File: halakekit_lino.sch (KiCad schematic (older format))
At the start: 8 parts, among them J1 HEADER_3, J2 HEADER_3, J3 HEADER_3, J4 HEADER_3, U1 BCM20737S

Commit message: Change board layout as rev 1.2
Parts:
- removed J1, J2, J3, J4: HEADER_3, simple_headers:Pin_Header_Straight_1x03_circle, symbol HEADER_3
- added J1: HEADER_10, simple_headers:Pin_Header_Straight_1x10, symbol HEADER_10
- 100u1: footprint Capacitors_SMD:C_0201 -> register_and_condensor:C_0603
- 10K1: footprint Resistors_SMD:R_0201 -> register_and_condensor:R_0603
- BT1: footprint CR2032_frame:BC-2001(CR2032 frame) -> CR2032_frame:BAT-HLD-001-TRCT
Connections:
- net GND: now also J1.5
- net RX: now also U1.31 (P2), J1.10; no longer U1.18 (UART_RX)
- net TX: now also U1.28 (P0), J1.9; no longer U1.19 (UART_TX)
- net VCC: now also J1.3
- net A1: now reaches U1.35 (P32)
- net A1: now also J1.8
- net AIO renamed A0
- net A0: now also J1.7
- net PIO0 renamed D0
- net D0: now also J1.6
- net PIO1 renamed D1
- net D1: now also J1.4
- net RST: no longer names the net of U1.27 (RESET_N)
- new net FWRX: J1.2, U1.18 (UART_RX)
- new net FWTX: J1.1, U1.19 (UART_TX)
- no-connect marks 17 -> 15
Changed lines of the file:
@@
 EESchema Schematic File Version 2
+LIBS:halakekit_lino-rescue
 LIBS:power
 LIBS:device
@@
 encoding utf-8
 Sheet 1 1
-Title ""
-Date ""
-Rev ""
-Comp ""
-Comment1 ""
+Title "HaLakeKit Lino"
+Date "2016-12-27"
+Rev "2.0"
+Comp "Nyampass.co.ltd"
+Comment1 "http://nyampass.com"
 Comment2 ""
 Comment3 ""
@@
 	1    0    0    -1
 $EndComp
-$Comp
-L BCM20737S U1
-U 1 1 583F77A8
-P 5100 2900
-F 0 "U1" H 5200 800 60  0000 C CNN
-F 1 "BCM20737S" H 5200 3300 60  0000 C CNN
-F 2 "BCM20737S:BCM20737S" H 5100 2900 60  0001 C CNN
-F 3 "" H 5100 2900 60  0000 C CNN
-	1    5100 2900
-	1    0    0    -1
-$EndComp
 Text GLabel 4550 4300 0    39   Input ~ 0
-RX
+FWRX
 Text GLabel 4550 4400 0    39   Input ~ 0
-TX
+FWTX
 NoConn ~ 5850 3600
 NoConn ~ 4550 3500
@@
 NoConn ~ 4550 4700
 NoConn ~ 5850 4800
-Text GLabel 5850 4700 2    39   Input ~ 0
-RST
 $Comp
 L GND #PWR02
@@
 F 0 "10K1" V 6180 4900 50  0000 C CNN
 F 1 "R" V 6100 4900 50  0000 C CNN
-F 2 "Resistors_SMD:R_0201" V 6030 4900 50  0001 C CNN
+F 2 "register_and_condensor:R_0603" V 6030 4900 50  0001 C CNN
 F 3 "" H 6100 4900 50  0000 C CNN
 	1    6100 4900
@@
 $EndComp
 Text GLabel 4550 2600 0    39   Input ~ 0
-PIO1
+D1
 Text GLabel 5850 3200 2    39   Input ~ 0
-PIO0
+D0
 Text GLabel 5850 3400 2    39   Input ~ 0
-AIO
+A0
 NoConn ~ 5850 3000
 NoConn ~ 5850 3100
-NoConn ~ 5850 3500
 NoConn ~ 5850 3700
 NoConn ~ 5850 3800
-NoConn ~ 5850 3900
-NoConn ~ 5850 4000
 NoConn ~ 5850 4100
 NoConn ~ 5850 4200
-NoConn ~ 5850 4300
 NoConn ~ 5850 4400
-NoConn ~ 5850 4600
 $Comp
 L VCC #PWR06
@@
 F 0 "100u1" H 7125 5000 50  0000 L CNN
 F 1 "C" H 7125 4800 50  0000 L CNN
-F 2 "Capacitors_SMD:C_0201" H 7138 4750 50  0001 C CNN
+F 2 "register_and_condensor:C_0603" H 7138 4750 50  0001 C CNN
 F 3 "" H 7100 4900 50  0000 C CNN
 	1    7100 4900
-	1    0    0    -1
-$EndComp
-$Comp
-L HEADER_3 J1
-U 1 1 583FB57F
-P 7700 3350
-F 0 "J1" H 7700 3550 60  0000 C CNN
-F 1 "HEADER_3" H 7700 3150 60  0000 C CNN
-F 2 "simple_headers:Pin_Header_Straight_1x03_circle" H 7700 3350 60  0001 C CNN
-F 3 "" H 7700 3350 60  0000 C CNN
-	1    7700 3350
 	1    0    0    -1
 $EndComp
@@
 F 0 "BT1" H 8050 4950 50  0000 L CNN
 F 1 "Battery" H 8050 4850 50  0000 L CNN
-F 2 "CR2032_frame:BC-2001(CR2032 frame)" V 7950 4940 50  0001 C CNN
+F 2 "CR2032_frame:BAT-HLD-001-TRCT" V 7950 4940 50  0001 C CNN
 F 3 "" V 7950 4940 50  0000 C CNN
 	1    7950 4900
@@
 	1    0    0    -1
 $EndComp
-$Comp
-L HEADER_3 J2
-U 1 1 583FB793
-P 7700 3950
-F 0 "J2" H 7700 4150 60  0000 C CNN
-F 1 "HEADER_3" H 7700 3750 60  0000 C CNN
-F 2 "simple_headers:Pin_Header_Straight_1x03_circle" H 7700 3950 60  0001 C CNN
-F 3 "" H 7700 3950 60  0000 C CNN
-	1    7700 3950
-	1    0    0    -1
-$EndComp
-$Comp
-L HEADER_3 J3
-U 1 1 583FB7D1
-P 8300 3350
-F 0 "J3" H 8300 3550 60  0000 C CNN
-F 1 "HEADER_3" H 8300 3150 60  0000 C CNN
-F 2 "simple_headers:Pin_Header_Straight_1x03_circle" H 8300 3350 60  0001 C CNN
-F 3 "" H 8300 3350 60  0000 C CNN
-	1    8300 3350
-	1    0    0    -1
-$EndComp
-$Comp
-L HEADER_3 J4
-U 1 1 583FB80E
-P 8600 3950
-F 0 "J4" H 8600 4150 60  0000 C CNN
-F 1 "HEADER_3" H 8600 3750 60  0000 C CNN
-F 2 "simple_headers:Pin_Header_Straight_1x03_circle" H 8600 3950 60  0001 C CNN
-F 3 "" H 8600 3950 60  0000 C CNN
-	1    8600 3950
-	1    0    0    -1
-$EndComp
-Text GLabel 7600 3450 0    39   Input ~ 0
+Text GLabel 8500 3150 0    39   Input ~ 0
+FWTX
+Text GLabel 8500 3250 0    39   Input ~ 0
+FWRX
+Text GLabel 8500 3750 0    39   Input ~ 0
+A0
+Text GLabel 8500 3850 0    39   Input ~ 0
+A1
+Text GLabel 8500 3950 0    39   Input ~ 0
 TX
-Text GLabel 7600 3350 0    39   Input ~ 0
-RX
-Text GLabel 7600 3250 0    39   Input ~ 0
-RST
-Text GLabel 8200 3250 0    39   Input ~ 0
-PIO1
-Text GLabel 8200 3350 0    39   Input ~ 0
-PIO0
-Text GLabel 8200 3450 0    39   Input ~ 0
-AIO
 $Comp
 L VCC #PWR010
 U 1 1 583FB8FE
-P 7300 3850
-F 0 "#PWR010" H 7300 3700 50  0001 C CNN
-F 1 "VCC" H 7300 4000 50  0000 C CNN
-F 2 "" H 7300 3850 50  0000 C CNN
-F 3 "" H 7300 3850 50  0000 C CNN
-	1    7300 3850
+P 8200 3350
+F 0 "#PWR010" H 8200 3200 50  0001 C CNN
+F 1 "VCC" H 8200 3500 50  0000 C CNN
+F 2 "" H 8200 3350 50  0000 C CNN
+F 3 "" H 8200 3350 50  0000 C CNN
+	1    8200 3350
 	1    0    0    -1
 $EndComp
 $Comp
 L GND #PWR011
-U 1 1 583FB954
-P 8300 4100
-F 0 "#PWR011" H 8300 3850 50  0001 C CNN
-F 1 "GND" H 8300 3950 50  0000 C CNN
-F 2 "" H 8300 4100 50  0000 C CNN
-F 3 "" H 8300 4100 50  0000 C CNN
-	1    8300 4100
-	1    0    0    -1
-$EndComp
-$Comp
-L VCC #PWR012
-U 1 1 583FB9BD
-P 8300 3850
-F 0 "#PWR012" H 8300 3700 50  0001 C CNN
-F 1 "VCC" H 8300 4000 50  0000 C CNN
-F 2 "" H 8300 3850 50  0000 C CNN
-F 3 "" H 8300 3850 50  0000 C CNN
-	1    8300 3850
-	1    0    0    -1
-$EndComp
-$Comp
-L GND #PWR013
 U 1 1 583FB9E0
-P 7300 4100
-F 0 "#PWR013" H 7300 3850 50  0001 C CNN
-F 1 "GND" H 7300 3950 50  0000 C CNN
-F 2 "" H 7300 4100 50  0000 C CNN
-F 3 "" H 7300 4100 50  0000 C CNN
-	1    7300 4100
+P 8200 3550
+F 0 "#PWR011" H 8200 3300 50  0001 C CNN
+F 1 "GND" H 8200 3400 50  0000 C CNN
+F 2 "" H 8200 3550 50  0000 C CNN
+F 3 "" H 8200 3550 50  0000 C CNN
+	1    8200 3550
 	1    0    0    -1
 $EndComp
@@
 	4550 2900 4200 2900
 Wire Wire Line
-	4550 3000 4200 3000
+	4200 3000 4550 3000
 Connection ~ 4200 3000
 Wire Wire Line
-	4550 3100 4200 3100
+	4200 3100 4550 3100
 Connection ~ 4200 3100
 Wire Wire Line
-	4550 3200 4200 3200
+	4200 3200 4550 3200
 Connection ~ 4200 3200
 Wire Wire Line
-	4550 3300 4200 3300
+	4200 3300 4550 3300
 Connection ~ 4200 3300
 Wire Wire Line
-	4550 3400 4200 3400
+	4200 3400 4550 3400
 Connection ~ 4200 3400
 Wire Wire Line
-	4550 3600 4200 3600
+	4200 3600 4550 3600
 Connection ~ 4200 3600
 Wire Wire Line
-	4550 3700 4200 3700
+	4200 3700 4550 3700
 Connection ~ 4200 3700
 Wire Wire Line
-	4550 3800 4200 3800
+	4200 3800 4550 3800
 Connection ~ 4200 3800
 Wire Wire Line
-	4550 3900 4200 3900
+	4200 3900 4550 3900
 Connection ~ 4200 3900
 Wire Wire Line
-	4550 4000 4200 4000
+	4200 4000 4550 4000
 Connection ~ 4200 4000
 Wire Wire Line
-	4550 4100 4200 4100
+	4200 4100 4550 4100
 Connection ~ 4200 4100
 Wire Wire Line
-	4550 4200 4200 4200
+	4200 4200 4550 4200
 Connection ~ 4200 4200
 Wire Wire Line
-	4200 2700 4200 5150
+	4200 2700 4200 2900
+Wire Wire Line
+	4200 2900 4200 3000
+Wire Wire Line
+	4200 3000 4200 3100
+Wire Wire Line
+	4200 3100 4200 3200
+Wire Wire Line
+	4200 3200 4200 3300
+Wire Wire Line
+	4200 3300 4200 3400
+Wire Wire Line
+	4200 3400 4200 3600
+Wire Wire Line
+	4200 3600 4200 3700
+Wire Wire Line
+	4200 3700 4200 3800
+Wire Wire Line
+	4200 3800 4200 3900
+Wire Wire Line
+	4200 3900 4200 4000
+Wire Wire Line
+	4200 4000 4200 4100
+Wire Wire Line
+	4200 4100 4200 4200
+Wire Wire Line
+	4200 4200 4200 4500
+Wire Wire Line
+	4200 4500 4200 4800
+Wire Wire Line
+	4200 4800 4200 4900
+Wire Wire Line
+	4200 4900 4200 5150
 Wire Wire Line
 	4550 4500 4200 4500
@@
 	5850 2600 6300 2600
 Wire Wire Line
-	6300 2600 6300 4600
+	6300 2600 6300 2700
+Wire Wire Line
+	6300 2700 6300 2800
+Wire Wire Line
+	6300 2800 6300 2900
+Wire Wire Line
+	6300 2900 6300 4500
+Wire Wire Line
+	6300 4500 6300 4600
 Wire Wire Line
 	5850 4500 6300 4500
@@
 	5850 3300 6450 3300
 Wire Wire Line
-	8300 3850 8500 3850
-Wire Wire Line
-	8500 3950 8300 3950
-Wire Wire Line
-	8300 3950 8300 4100
-Wire Wire Line
-	8500 4050 8300 4050
-Connection ~ 8300 4050
-Wire Wire Line
-	7600 3850 7300 3850
-Wire Wire Line
-	7600 3950 7300 3950
-Wire Wire Line
-	7300 3950 7300 4100
-Wire Wire Line
-	7600 4050 7300 4050
-Connection ~ 7300 4050
+	8500 3350 8200 3350
+$Comp
+L HEADER_10 J1
+U 1 1 58611085
+P 8600 3600
+F 0 "J1" H 8600 4150 60  0000 C CNN
+F 1 "HEADER_10" H 8600 3050 60  0000 C CNN
+F 2 "simple_headers:Pin_Header_Straight_1x10" H 8600 3600 60  0001 C CNN
+F 3 "" H 8600 3600 60  0000 C CNN
+	1    8600 3600
+	1    0    0    -1
+$EndComp
+Wire Wire Line
+	8500 3550 8200 3550
+Text GLabel 5850 3900 2    39   Input ~ 0
+A1
+Text GLabel 8500 4050 0    39   Input ~ 0
+RX
+NoConn ~ 5850 4700
+Text GLabel 8500 3450 0    39   Input ~ 0
+D1
+Text GLabel 8500 3650 0    39   Input ~ 0
+D0
+$Comp
+L BCM20737S U1
+U 1 1 5861DFC0
+P 5100 2900
+F 0 "U1" H 5200 800 60  0000 C CNN
+F 1 "BCM20737S" H 5200 3300 60  0000 C CNN
+F 2 "BCM20737S:BCM20737S" H 5100 2900 60  0001 C CNN
+F 3 "" H 5100 2900 60  0000 C CNN
+	1    5100 2900
+	1    0    0    -1
+$EndComp
+Text GLabel 5850 4600 2    39   Input ~ 0
+TX
+Text GLabel 5850 4300 2    39   Input ~ 0
+RX
+NoConn ~ 5850 3500
+NoConn ~ 5850 4000
 $EndSCHEMATC

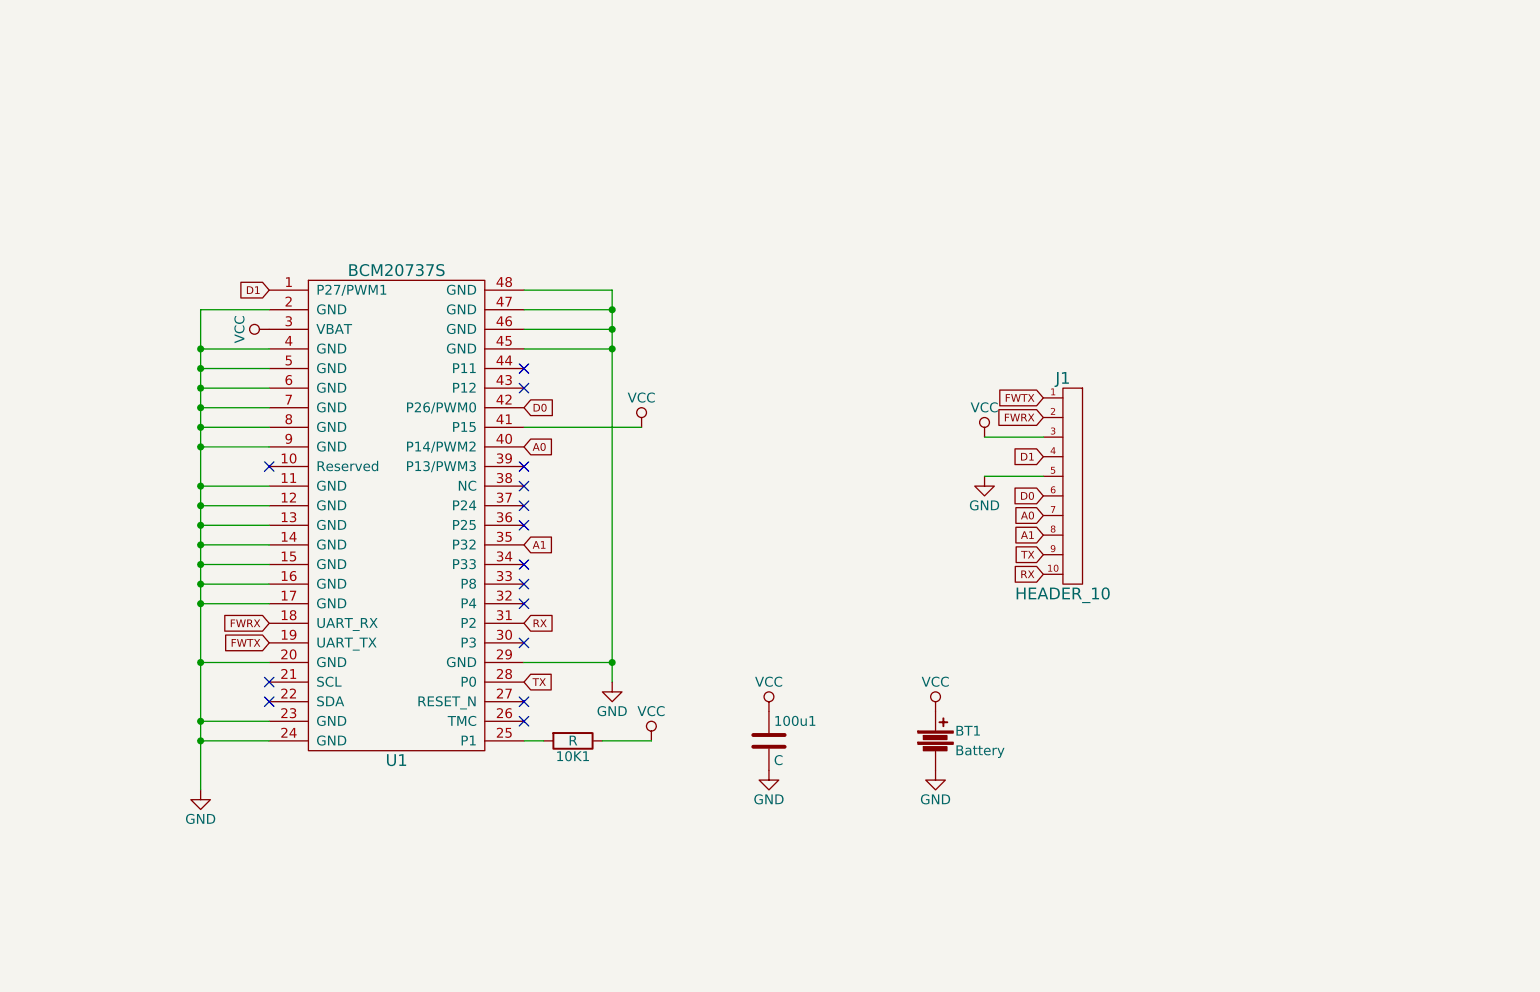
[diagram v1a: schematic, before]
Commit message: Create net data with using MDBT40
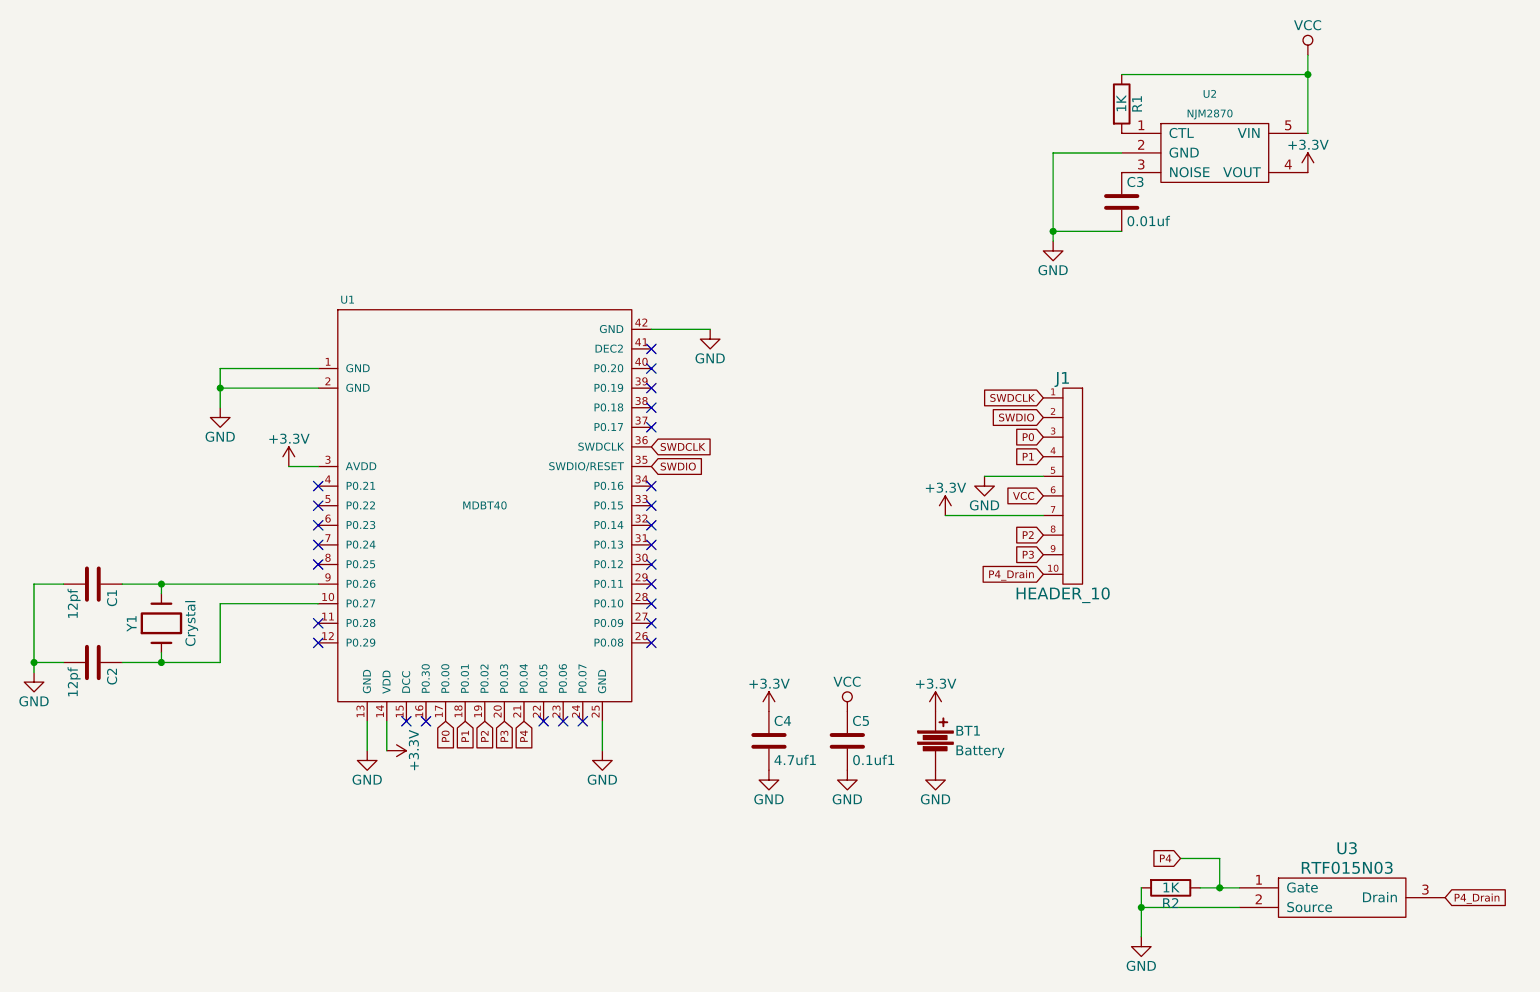
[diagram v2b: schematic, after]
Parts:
- removed 10K1: R, register_and_condensor:R_0603, symbol R
- removed U1: BCM20737S, BCM20737S:BCM20737S, symbol BCM20737S
- added C1, C2: 12pf, register_and_condensor:C_0603, symbol C
- added C3: 0.01uf, register_and_condensor:C_0603, symbol C
- added C5: 0.1uf1, register_and_condensor:C_0603, symbol C
- added R1, R2: 1K, register_and_condensor:R_0603, symbol R
- added U1: MDBT40, MDBT40:MDBT40, symbol MDBT40
- added U2: NJM2870, common:SOT-23-5, symbol NJM2870
- added U3: RTF015N03, mosfet:rtf015n03, symbol RTF015N03
- added Y1: Crystal, common:FC-135, symbol Crystal
- C4: renamed from 100u1; value C -> 4.7uf1; footprint register_and_condensor:C_0603 -> Capacitors_SMD:C_1812
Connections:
- net D0 is gone; now on net VCC: J1.6
- net GND: now also C1.2, C2.2, C3.2, C5.2, R2.2, U1.1 (GND), U1.13 (GND), U1.2 (GND), U1.25 (GND), U1.42 (GND), U2.2 (GND), U3.2 (Source)
- net VCC: now also C5.1, R1.1, U2.5 (VIN); no longer BT1.1, C4.1, J1.3
- net A0 renamed +3V3
- net +3V3: now also BT1.1, C4.1, U1.14 (VDD), U1.3 (AVDD), U2.4 (VOUT)
- net A1 renamed P2
- net P2: now also U1.19 (P0.02)
- net D1 renamed P1
- net P1: now also U1.18 (P0.01)
- net FWRX renamed SWDIO
- net SWDIO: now also U1.35 (SWDIO/RESET)
- net FWTX renamed SWDCLK
- net SWDCLK: now also U1.36 (SWDCLK)
- net RX renamed P4_Drain
- net P4_Drain: now also U3.3 (Drain)
- net TX renamed P3
- net P3: now also U1.20 (P0.03)
- new net: C2.1, U1.10 (P0.27), Y1.1
- new net: C1.1, U1.9 (P0.26), Y1.2
- new net: R1.2, U2.1 (CTL)
- new net: C3.1, U2.3 (NOISE)
- new net P0: J1.3, U1.17 (P0.00)
- new net P4: R2.1, U1.21 (P0.04), U3.1 (Gate)
- no-connect marks 15 -> 26
